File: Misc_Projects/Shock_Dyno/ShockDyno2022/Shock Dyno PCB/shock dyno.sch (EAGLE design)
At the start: 29 parts, among them IC1 ADS8332IBPWR, K1 T9GS1L14-5, U1 REF5040AIDR

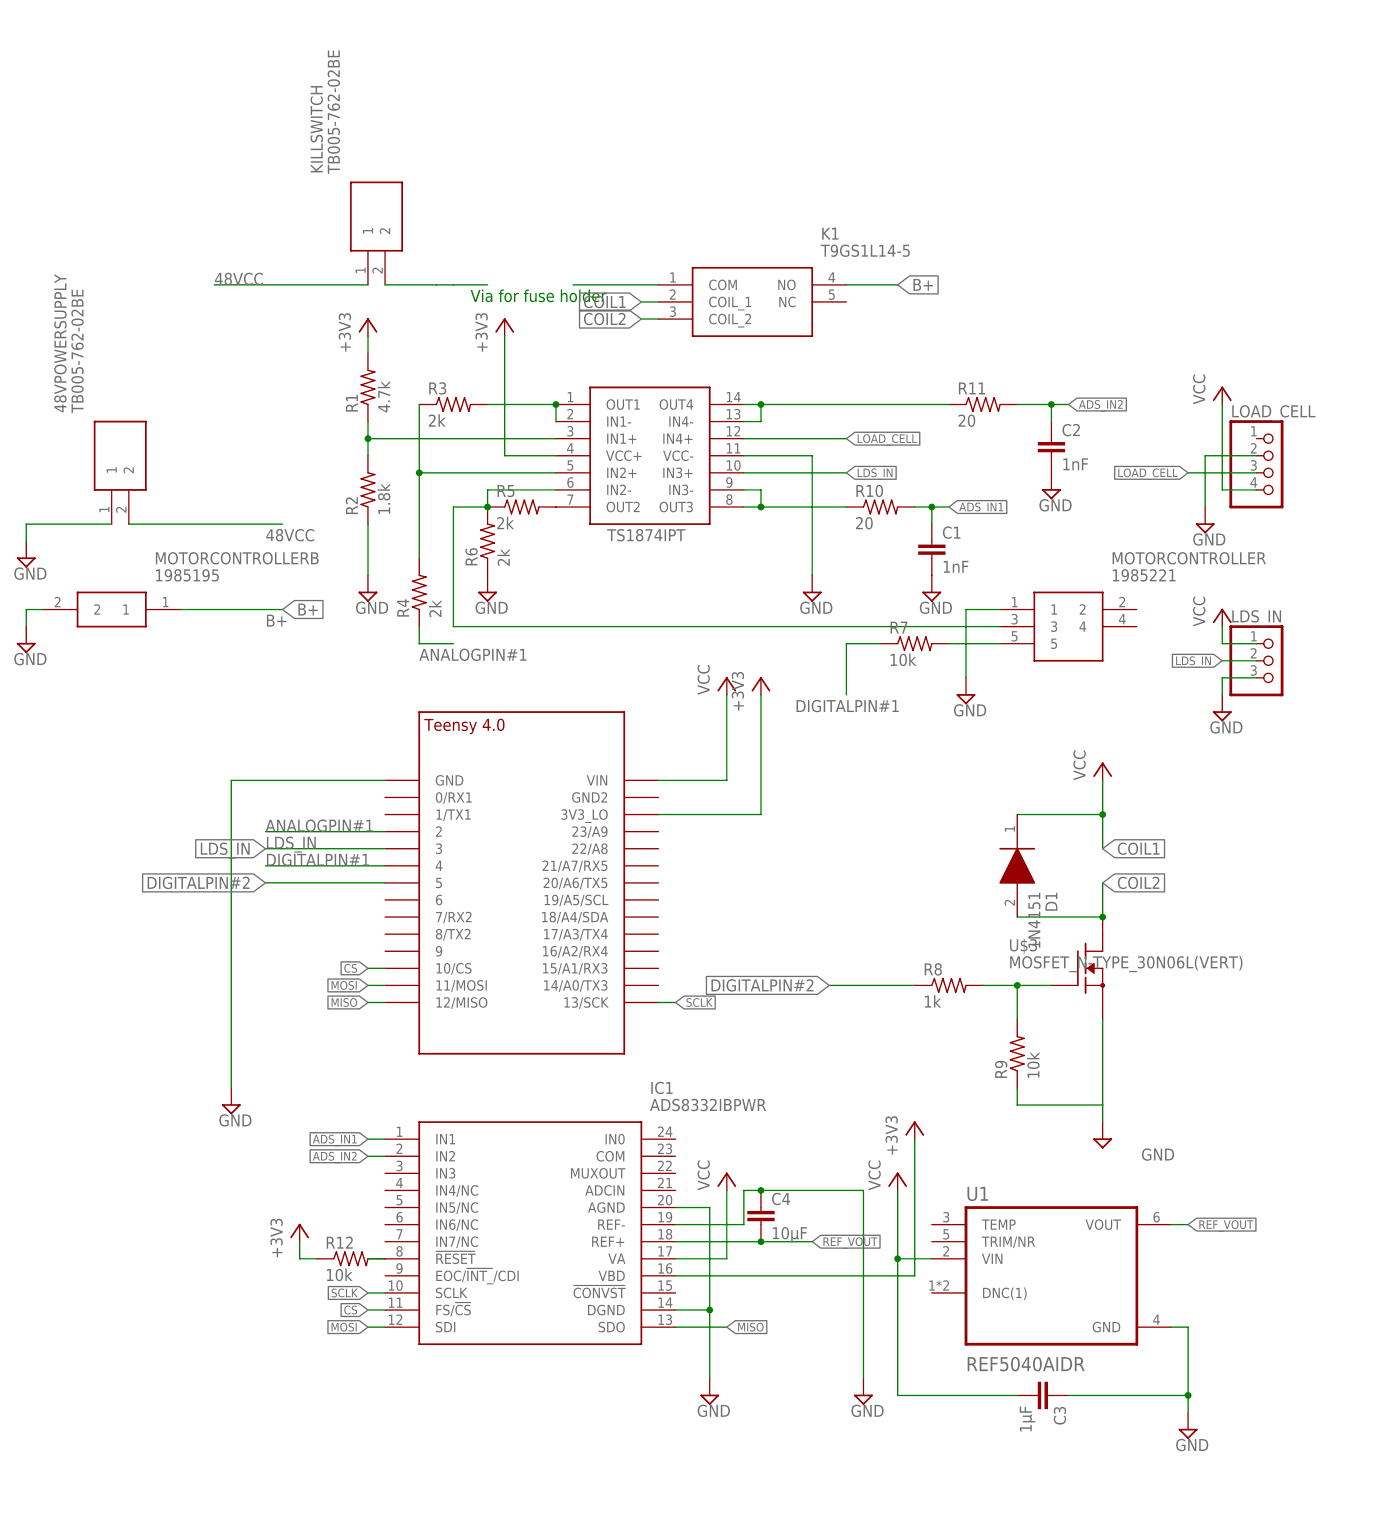
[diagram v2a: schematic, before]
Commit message: added brd file to shock dyno
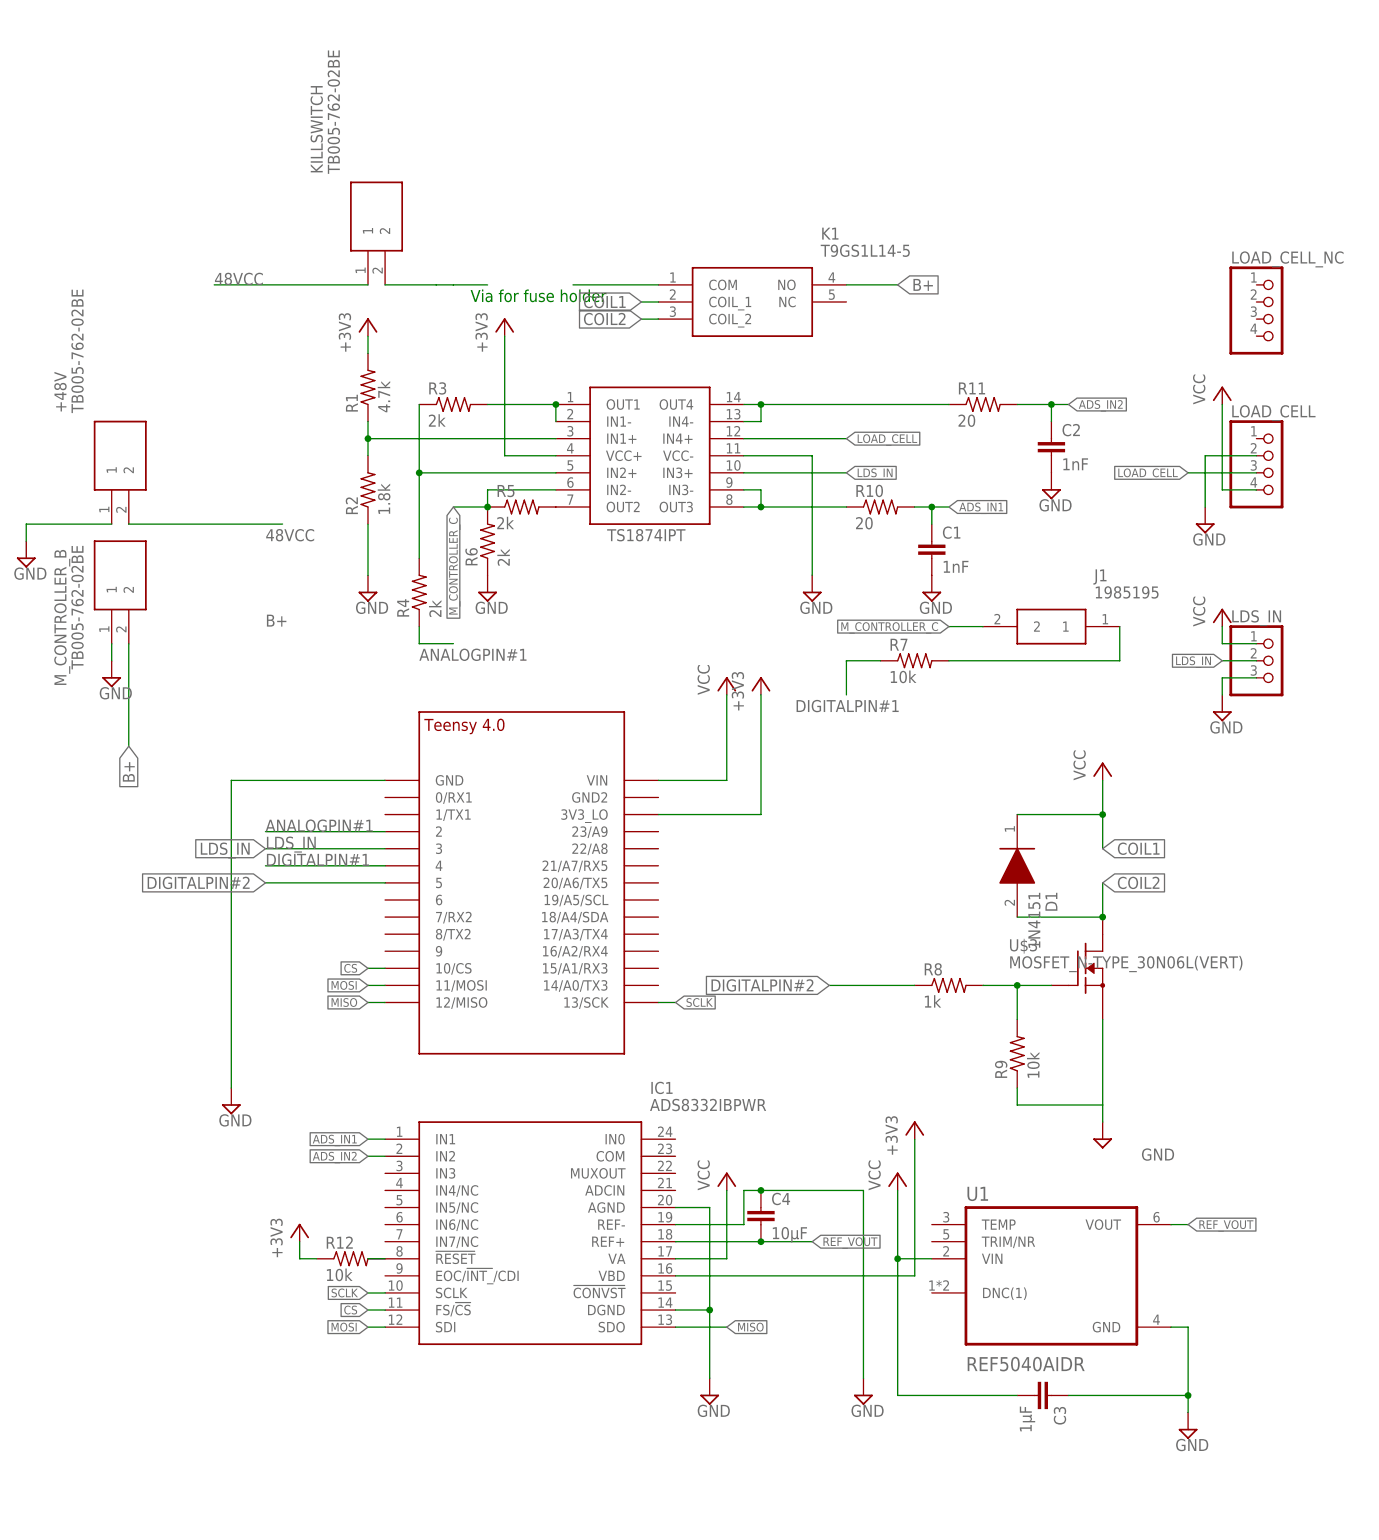
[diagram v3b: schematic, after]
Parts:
- removed MOTORCONTROLLER: 1985221, 1985221:1985221
- removed MOTORCONTROLLERB: 1985195, 1985195:1985195
- added J1: 1985195, GTOR - Connectors:1985195
- added LOAD_CELL_NC: (no value), GTOR - Connectors:PINHD-1X4
- added M_CONTROLLER_B: TB005-762-02BE, GTOR - Connectors:TB005-762-02BE
- renumbered 48VPOWERSUPPLY to +48V
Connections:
- removed net N$5: MOTORCONTROLLER.3, R5.1, R6.2, U$1.IN2-
- new net M_CONTROLLER_C: J1.2, R5.1, R6.2, U$1.IN2-
- net B+: now also M_CONTROLLER_B.2; no longer MOTORCONTROLLERB.1
- net GND: now also M_CONTROLLER_B.1; no longer MOTORCONTROLLER.1, MOTORCONTROLLERB.2
- net N$7: now also J1.1; no longer MOTORCONTROLLER.5
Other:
- moved on the sheet: R7
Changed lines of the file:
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@@
 <part name="R6" library="GTOR - Passive Components" deviceset="RES_SMD" device="R0603" package3d_urn="urn:adsk.eagle:package:23555/3" value="2k"/>
 <part name="SUPPLY4" library="GTOR - Documation Frame" deviceset="GND" device=""/>
-<part name="SUPPLY5" library="GTOR - Documation Frame" deviceset="GND" device=""/>
 <part name="R7" library="GTOR - Passive Components" deviceset="RES_SMD" device="R0603" package3d_urn="urn:adsk.eagle:package:23555/3" value="10k"/>
-<part name="MOTORCONTROLLERB" library="1985195" deviceset="1985195" device=""/>
-<part name="MOTORCONTROLLER" library="1985221" deviceset="1985221" device=""/>
 <part name="SUPPLY7" library="GTOR - Documation Frame" deviceset="GND" device=""/>
 <part name="SUPPLY8" library="GTOR - Documation Frame" deviceset="GND" device=""/>
-<part name="48VPOWERSUPPLY" library="GTOR - Connectors" deviceset="TB005-762-02BE" device=""/>
+<part name="+48V" library="GTOR - Connectors" deviceset="TB005-762-02BE" device=""/>
 <part name="KILLSWITCH" library="GTOR - Connectors" deviceset="TB005-762-02BE" device=""/>
 <part name="K1" library="GTOR - Active Components" deviceset="T9GS1L14-5" device=""/>
@@
 <part name="+3V4" library="GTOR - Documation Frame" deviceset="+3V3" device=""/>
 <part name="+3V5" library="GTOR - Documation Frame" deviceset="+3V3" device=""/>
+<part name="LOAD_CELL_NC" library="GTOR - Connectors" deviceset="PINHD-1X4" device="" package3d_urn="urn:adsk.eagle:package:22407/2"/>
+<part name="M_CONTROLLER_B" library="GTOR - Connectors" deviceset="TB005-762-02BE" device=""/>
+<part name="J1" library="GTOR - Connectors" deviceset="1985195" device=""/>
 </parts>
 <sheets>
@@
 <attribute name="VALUE" x="10.795" y="34.925" size="1.778" layer="96"/>
 </instance>
-<instance part="SUPPLY5" gate="GND" x="83.82" y="22.86" smashed="yes">
-<attribute name="VALUE" x="81.915" y="19.685" size="1.778" layer="96"/>
-</instance>
-<instance part="R7" gate="G$1" x="76.2" y="30.48" smashed="yes">
-<attribute name="NAME" x="72.39" y="31.9786" size="1.778" layer="95"/>
-<attribute name="VALUE" x="72.39" y="27.178" size="1.778" layer="96"/>
-</instance>
-<instance part="MOTORCONTROLLERB" gate="G$1" x="-53.34" y="35.56" smashed="yes">
-<attribute name="NAME" x="-36.83" y="43.18" size="1.778" layer="95" align="center-left"/>
-<attribute name="VALUE" x="-36.83" y="40.64" size="1.778" layer="96" align="center-left"/>
-</instance>
-<instance part="MOTORCONTROLLER" gate="G$1" x="88.9" y="35.56" smashed="yes">
-<attribute name="NAME" x="105.41" y="43.18" size="1.778" layer="95" align="center-left"/>
-<attribute name="VALUE" x="105.41" y="40.64" size="1.778" layer="96" align="center-left"/>
+<instance part="R7" gate="G$1" x="76.2" y="27.94" smashed="yes">
+<attribute name="NAME" x="72.39" y="29.4386" size="1.778" layer="95"/>
+<attribute name="VALUE" x="72.39" y="24.638" size="1.778" layer="96"/>
 </instance>
 <instance part="SUPPLY7" gate="GND" x="-55.88" y="43.18" smashed="yes">
 <attribute name="VALUE" x="-57.785" y="40.005" size="1.778" layer="96"/>
 </instance>
-<instance part="SUPPLY8" gate="GND" x="-55.88" y="30.48" smashed="yes">
-<attribute name="VALUE" x="-57.785" y="27.305" size="1.778" layer="96"/>
-</instance>
-<instance part="48VPOWERSUPPLY" gate="G$1" x="-43.18" y="48.26" smashed="yes" rot="R90">
+<instance part="SUPPLY8" gate="GND" x="-43.18" y="25.4" smashed="yes">
+<attribute name="VALUE" x="-45.085" y="22.225" size="1.778" layer="96"/>
+</instance>
+<instance part="+48V" gate="G$1" x="-43.18" y="48.26" smashed="yes" rot="R90">
 <attribute name="NAME" x="-50.8" y="64.77" size="1.778" layer="95" rot="R90" align="center-left"/>
 <attribute name="VALUE" x="-48.26" y="64.77" size="1.778" layer="96" rot="R90" align="center-left"/>
@@
 <instance part="+3V5" gate="G$1" x="15.24" y="78.74" smashed="yes">
 <attribute name="VALUE" x="12.7" y="73.66" size="1.778" layer="96" rot="R90"/>
+</instance>
+<instance part="LOAD_CELL_NC" gate="A" x="129.54" y="78.74" smashed="yes">
+<attribute name="NAME" x="123.19" y="86.995" size="1.778" layer="95"/>
+<attribute name="VALUE" x="123.19" y="71.12" size="1.778" layer="96"/>
+</instance>
+<instance part="M_CONTROLLER_B" gate="G$1" x="-43.18" y="30.48" smashed="yes" rot="R90">
+<attribute name="NAME" x="-50.8" y="24.13" size="1.778" layer="95" rot="R90" align="center-left"/>
+<attribute name="VALUE" x="-48.26" y="26.67" size="1.778" layer="96" rot="R90" align="center-left"/>
+</instance>
+<instance part="J1" gate="G$1" x="86.36" y="33.02" smashed="yes">
+<attribute name="NAME" x="102.87" y="40.64" size="1.778" layer="95" align="center-left"/>
+<attribute name="VALUE" x="102.87" y="38.1" size="1.778" layer="96" align="center-left"/>
 </instance>
 </instances>
@@
 </segment>
 <segment>
-<wire x1="88.9" y1="35.56" x2="83.82" y2="35.56" width="0.1524" layer="91"/>
-<wire x1="83.82" y1="35.56" x2="83.82" y2="25.4" width="0.1524" layer="91"/>
-<pinref part="SUPPLY5" gate="GND" pin="GND"/>
-<pinref part="MOTORCONTROLLER" gate="G$1" pin="1"/>
-</segment>
-<segment>
 <pinref part="SUPPLY7" gate="GND" pin="GND"/>
 <wire x1="-55.88" y1="48.26" x2="-55.88" y2="45.72" width="0.1524" layer="91"/>
-<pinref part="48VPOWERSUPPLY" gate="G$1" pin="1"/>
+<pinref part="+48V" gate="G$1" pin="1"/>
 <wire x1="-55.88" y1="48.26" x2="-43.18" y2="48.26" width="0.1524" layer="91"/>
-</segment>
-<segment>
-<pinref part="MOTORCONTROLLERB" gate="G$1" pin="2"/>
-<wire x1="-53.34" y1="35.56" x2="-55.88" y2="35.56" width="0.1524" layer="91"/>
-<wire x1="-55.88" y1="35.56" x2="-55.88" y2="33.02" width="0.1524" layer="91"/>
-<pinref part="SUPPLY8" gate="GND" pin="GND"/>
 </segment>
 <segment>
@@
 <wire x1="121.92" y1="25.4" x2="121.92" y2="22.86" width="0.1524" layer="91"/>
 </segment>
+<segment>
+<pinref part="M_CONTROLLER_B" gate="G$1" pin="1"/>
+<pinref part="SUPPLY8" gate="GND" pin="GND"/>
+<wire x1="-43.18" y1="30.48" x2="-43.18" y2="27.94" width="0.1524" layer="91"/>
+</segment>
 </net>
 <net name="+3V3" class="0">
@@
 </segment>
 </net>
-<net name="N$5" class="0">
-<segment>
-<pinref part="R5" gate="G$1" pin="1"/>
-<pinref part="U$1" gate="G$1" pin="IN2-"/>
-<wire x1="12.7" y1="50.8" x2="12.7" y2="53.34" width="0.1524" layer="91"/>
-<wire x1="12.7" y1="53.34" x2="22.86" y2="53.34" width="0.1524" layer="91"/>
-<pinref part="R6" gate="G$1" pin="2"/>
-<junction x="12.7" y="50.8"/>
-<wire x1="12.7" y1="50.8" x2="7.62" y2="50.8" width="0.1524" layer="91"/>
-<wire x1="7.62" y1="50.8" x2="7.62" y2="33.02" width="0.1524" layer="91"/>
-<wire x1="7.62" y1="33.02" x2="88.9" y2="33.02" width="0.1524" layer="91"/>
-<pinref part="MOTORCONTROLLER" gate="G$1" pin="3"/>
-</segment>
-</net>
-<net name="N$7" class="0">
-<segment>
-<pinref part="R7" gate="G$1" pin="2"/>
-<wire x1="88.9" y1="30.48" x2="81.28" y2="30.48" width="0.1524" layer="91"/>
-<pinref part="MOTORCONTROLLER" gate="G$1" pin="5"/>
-</segment>
-</net>
 <net name="DIGITALPIN#1" class="0">
 <segment>
+<label x="58.42" y="20.32" size="1.778" layer="95"/>
 <pinref part="R7" gate="G$1" pin="1"/>
-<wire x1="71.12" y1="30.48" x2="66.04" y2="30.48" width="0.1524" layer="91"/>
-<wire x1="66.04" y1="30.48" x2="66.04" y2="22.86" width="0.1524" layer="91"/>
-<label x="58.42" y="20.32" size="1.778" layer="95"/>
+<wire x1="66.04" y1="27.94" x2="66.04" y2="22.86" width="0.1524" layer="91"/>
+<wire x1="71.12" y1="27.94" x2="66.04" y2="27.94" width="0.1524" layer="91"/>
 </segment>
 <segment>
@@
 <wire x1="-40.64" y1="48.26" x2="-17.78" y2="48.26" width="0.1524" layer="91"/>
 <label x="-20.32" y="45.72" size="1.778" layer="95"/>
-<pinref part="48VPOWERSUPPLY" gate="G$1" pin="2"/>
+<pinref part="+48V" gate="G$1" pin="2"/>
 </segment>
 <segment>
@@
 <net name="B+" class="0">
 <segment>
-<pinref part="MOTORCONTROLLERB" gate="G$1" pin="1"/>
-<wire x1="-33.02" y1="35.56" x2="-17.78" y2="35.56" width="0.1524" layer="91"/>
+<wire x1="-40.64" y1="30.48" x2="-40.64" y2="15.24" width="0.1524" layer="91"/>
 <label x="-20.32" y="33.02" size="1.778" layer="95"/>
-<label x="-17.78" y="35.56" size="1.778" layer="95" xref="yes"/>
+<label x="-40.64" y="15.24" size="1.778" layer="95" rot="R270" xref="yes"/>
+<pinref part="M_CONTROLLER_B" gate="G$1" pin="2"/>
 </segment>
 <segment>
@@
 </segment>
 </net>
+<net name="N$7" class="0">
+<segment>
+<wire x1="81.28" y1="27.94" x2="106.68" y2="27.94" width="0.1524" layer="91"/>
+<wire x1="106.68" y1="27.94" x2="106.68" y2="33.02" width="0.1524" layer="91"/>
+<pinref part="R7" gate="G$1" pin="2"/>
+<pinref part="J1" gate="G$1" pin="1"/>
+</segment>
+</net>
+<net name="M_CONTROLLER_C" class="0">
+<segment>
+<wire x1="86.36" y1="33.02" x2="81.28" y2="33.02" width="0.1524" layer="91"/>
+<label x="81.28" y="33.02" size="1.27" layer="95" rot="R180" xref="yes"/>
+<pinref part="J1" gate="G$1" pin="2"/>
+</segment>
+<segment>
+<pinref part="R5" gate="G$1" pin="1"/>
+<pinref part="U$1" gate="G$1" pin="IN2-"/>
+<wire x1="12.7" y1="50.8" x2="12.7" y2="53.34" width="0.1524" layer="91"/>
+<wire x1="12.7" y1="53.34" x2="22.86" y2="53.34" width="0.1524" layer="91"/>
+<pinref part="R6" gate="G$1" pin="2"/>
+<junction x="12.7" y="50.8"/>
+<wire x1="12.7" y1="50.8" x2="7.62" y2="50.8" width="0.1524" layer="91"/>
+<label x="7.62" y="50.8" size="1.27" layer="95" rot="R270" xref="yes"/>
+</segment>
+</net>
